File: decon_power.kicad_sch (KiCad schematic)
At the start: 0 parts

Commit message: modified:   DECON_Ctrl_Panel.kicad_pcb 	modified:   DECON_Ctrl_Panel.kicad_prl 	new file:   MCU_pins.xlsx 	new file:   Son_KiCad_lib/Son_KiCad_lib.bak 	new file:   Son_KiCad_lib/Son_KiCad_lib.kicad_sym 	new file:   Son_KiCad_lib/Son_KiCad_lib.pretty/URB2405YMD-10WR3.kicad_mod 	modified:   decon_input.kicad_sch 	modified:   decon_mcu.kicad_sch 	modified:   decon_output.kicad_sch 	modified:   decon_power.kicad_sch 	new file:   fp-lib-table 	new file:   sym-lib-table
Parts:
- added J23: Conn_01x02, symbol Connector_Generic:Conn_01x02
- added U1: URB2405YMD-10WR3, Son_KiCad_lib:URB2405YMD-10WR3, symbol Son_KiCad_lib:URB2405YMD-10WR3
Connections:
- new net: J23.2 (Pin_2), U1.1 (-VIN)
- new net 5V: U1.3 (+VOUT)
- new net MCU_GND: U1.5 (-VOUT)
- new net VBATT: J23.1 (Pin_1), U1.2 (+VIN)

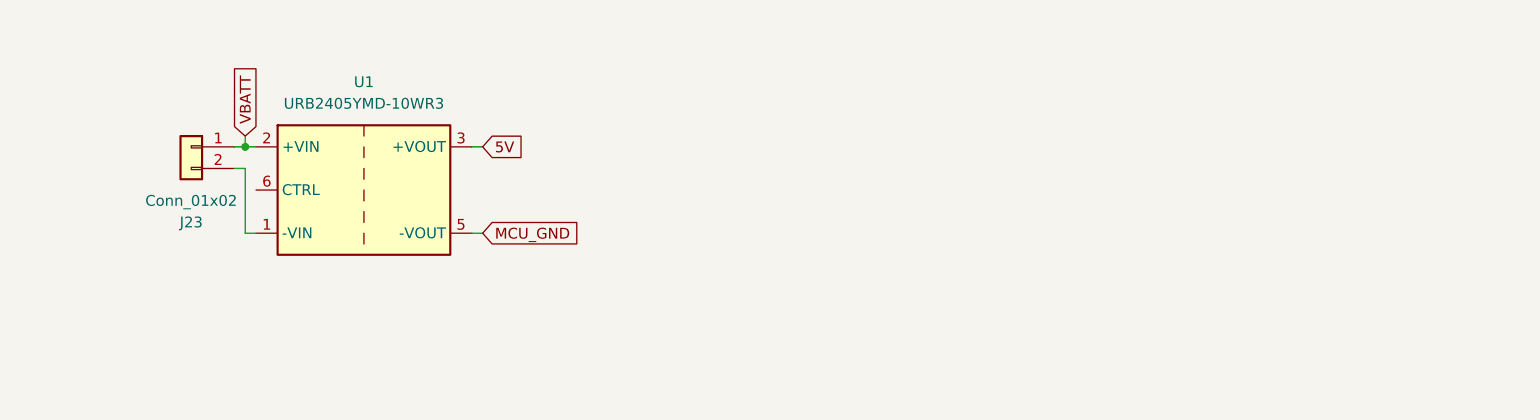
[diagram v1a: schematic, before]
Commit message: modified:   DECON_Ctrl_Panel.kicad_sch
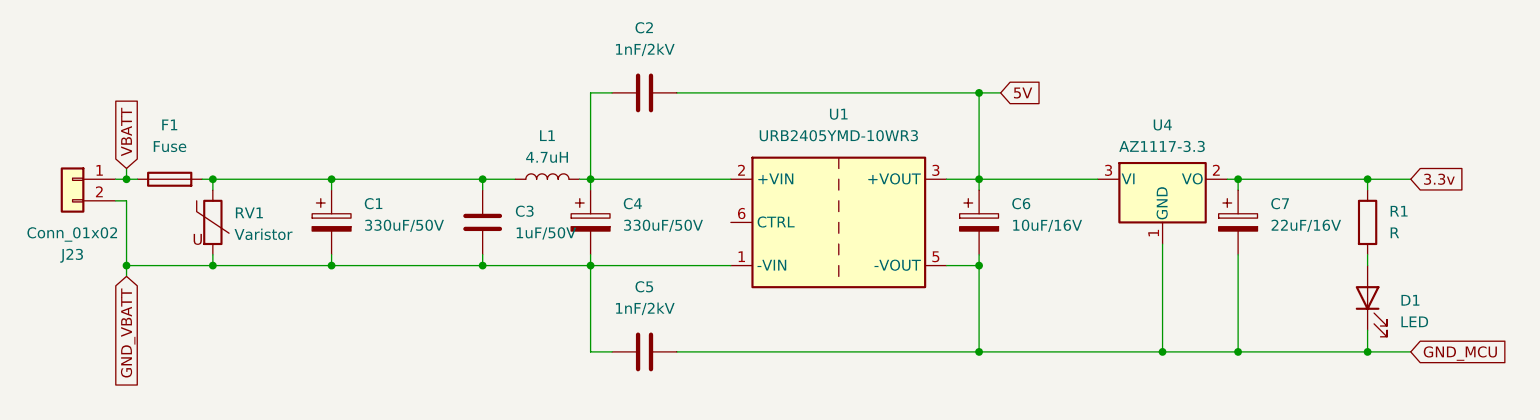
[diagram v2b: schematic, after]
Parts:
- added C1, C4: 330uF/50V, Capacitor_SMD:CP_Elec_10x10.5, symbol Device:C_Polarized
- added C2, C5: 1nF/2kV, Capacitor_THT:C_Disc_D5.0mm_W2.5mm_P5.00mm, symbol Device:C
- added C3: 1uF/50V, Capacitor_SMD:C_0805_2012Metric, symbol Device:C
- added C6: 10uF/16V, Capacitor_SMD:CP_Elec_4x5.4, symbol Device:C_Polarized
- added C7: 22uF/16V, Capacitor_SMD:CP_Elec_4x5.4, symbol Device:C_Polarized
- added D1: LED, LED_SMD:LED_0805_2012Metric, symbol Device:LED
- added F1: Fuse, Fuse:Fuseholder_Clip-5x20mm_Eaton_1A5601-01_Inline_P20.80x6.76mm_D1.70mm_Horizontal, symbol Device:Fuse
- added L1: 4.7uH, Inductor_SMD:L_APV_APH0630, symbol Device:L
- added R1: R, Resistor_SMD:R_0805_2012Metric, symbol Device:R
- added RV1: Varistor, Varistor:RV_Disc_D7mm_W3.4mm_P5mm, symbol Device:Varistor
- added U4: AZ1117-3.3, Package_TO_SOT_SMD:SOT-223-3_TabPin2, symbol Regulator_Linear:AZ1117-3.3
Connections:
- net 5V: now also C2.2, C6.1, U4.3 (VI)
- net VBATT: now also F1.1; no longer U1.2 (+VIN)
- net GND_VBATT: now reaches J23.2 (Pin_2), U1.1 (-VIN)
- net GND_VBATT: now also C1.2, C3.2, C4.2, C5.1, RV1.2
- net MCU_GND renamed GND_MCU
- net GND_MCU: now also C5.2, C6.2, C7.2, D1.1 (K), U4.1 (GND)
- new net: C2.1, C4.1, L1.2, U1.2 (+VIN)
- new net: C1.1, C3.1, F1.2, L1.1, RV1.1
- new net: D1.2 (A), R1.2
- new net 3.3v: C7.1, R1.1, U4.2 (VO)
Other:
- moved on the sheet: J23, U1

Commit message: new file:   decon_ctrl.pdf
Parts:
- removed C1, C4: 330uF/50V, Capacitor_SMD:CP_Elec_10x10.5, symbol Device:C_Polarized
- removed C2, C5: 1nF/2kV, Capacitor_THT:C_Disc_D5.0mm_W2.5mm_P5.00mm, symbol Device:C
- removed C3: 1uF/50V, Capacitor_SMD:C_0805_2012Metric, symbol Device:C
- removed C6: 10uF/16V, Capacitor_SMD:CP_Elec_4x5.4, symbol Device:C_Polarized
- removed C7: 22uF/16V, Capacitor_SMD:CP_Elec_4x5.4, symbol Device:C_Polarized
- removed D1: LED, LED_SMD:LED_0805_2012Metric, symbol Device:LED
- removed F1: Fuse, Fuse:Fuseholder_Clip-5x20mm_Eaton_1A5601-01_Inline_P20.80x6.76mm_D1.70mm_Horizontal, symbol Device:Fuse
- removed J23: Conn_01x02, symbol Connector_Generic:Conn_01x02
- removed L1: 4.7uH, Inductor_SMD:L_APV_APH0630, symbol Device:L
- removed R1: R, Resistor_SMD:R_0805_2012Metric, symbol Device:R
- removed RV1: Varistor, Varistor:RV_Disc_D7mm_W3.4mm_P5mm, symbol Device:Varistor
- removed U1: URB2405YMD-10WR3, Son_KiCad_lib:URB2405YMD-10WR3, symbol Son_KiCad_lib:URB2405YMD-10WR3
- removed U4: AZ1117-3.3, Package_TO_SOT_SMD:SOT-223-3_TabPin2, symbol Regulator_Linear:AZ1117-3.3
